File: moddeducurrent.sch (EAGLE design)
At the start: 29 parts, among them IC1 TLC251D, IC2 LMV321M5X, X1 USBPCB, X2 USBOLD

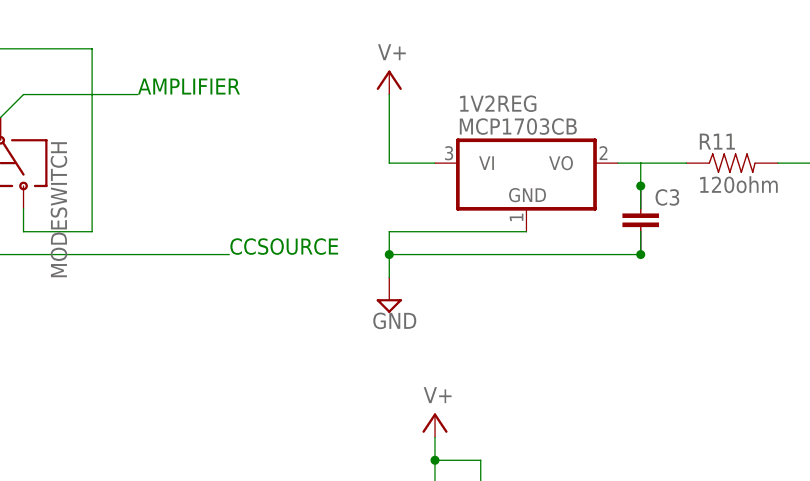
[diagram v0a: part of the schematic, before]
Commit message: Added missing input capacitor on 1V2REG just in case, fixed a piee of atrocious routing on the output cap of the same, beefed up the main current carrying trace.
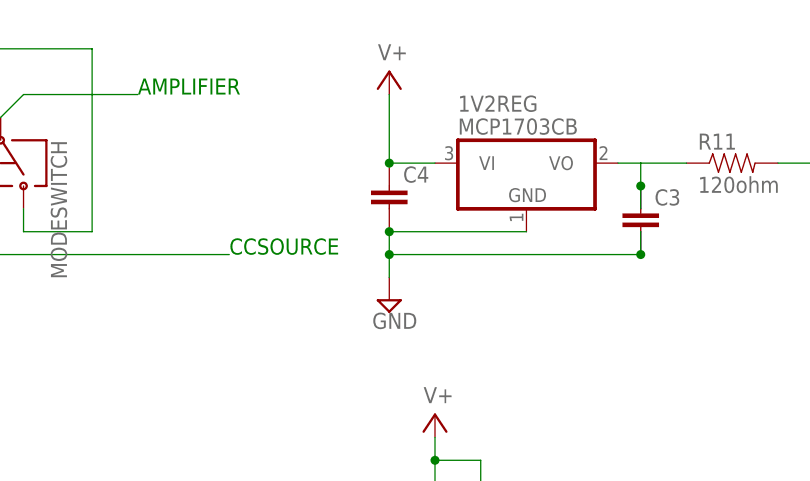
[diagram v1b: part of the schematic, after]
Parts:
- added C4: (no value), SparkFun - Copy:CAP0805
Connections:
- net GND: now also C4.2
- net V+: now also C4.1
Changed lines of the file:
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@@
 <part name="R12" library="SparkFun - Copy" deviceset="RESISTOR" device="0805-RES"/>
 <part name="S1" library="LL" deviceset="SWITCH-DP3T" device=""/>
+<part name="C4" library="SparkFun - Copy" deviceset="CAP" device="0805"/>
 </parts>
 <sheets>
@@
 <instance part="R12" gate="G$1" x="-27.94" y="101.6"/>
 <instance part="S1" gate="G$1" x="58.42" y="43.18"/>
+<instance part="C4" gate="G$1" x="132.08" y="121.92"/>
 </instances>
 <busses>
@@
 <pinref part="1V2REG" gate="G$1" pin="GND"/>
 <pinref part="SUPPLY10" gate="GND" pin="GND"/>
+<pinref part="C4" gate="G$1" pin="2"/>
+<junction x="132.08" y="119.38"/>
 </segment>
 <segment>
@@
 <pinref part="1V2REG" gate="G$1" pin="VI"/>
 <pinref part="SUPPLY7" gate="1" pin="V+"/>
-</segment>
-</net>
+<pinref part="C4" gate="G$1" pin="1"/>
+<junction x="132.08" y="127"/>
+</segment>
+</net>

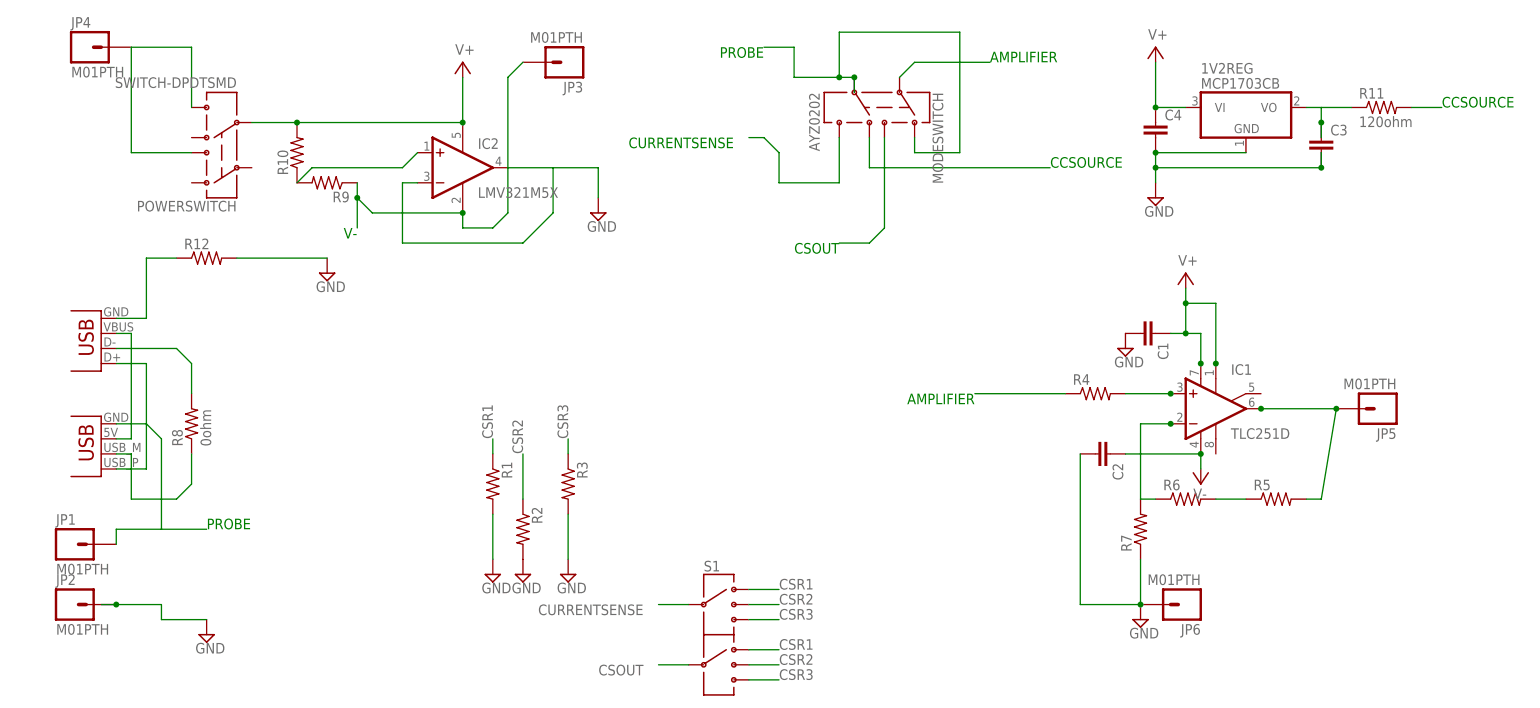
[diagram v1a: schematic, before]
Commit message: Changed switch to cheaper ebay switch. Added signal plane.
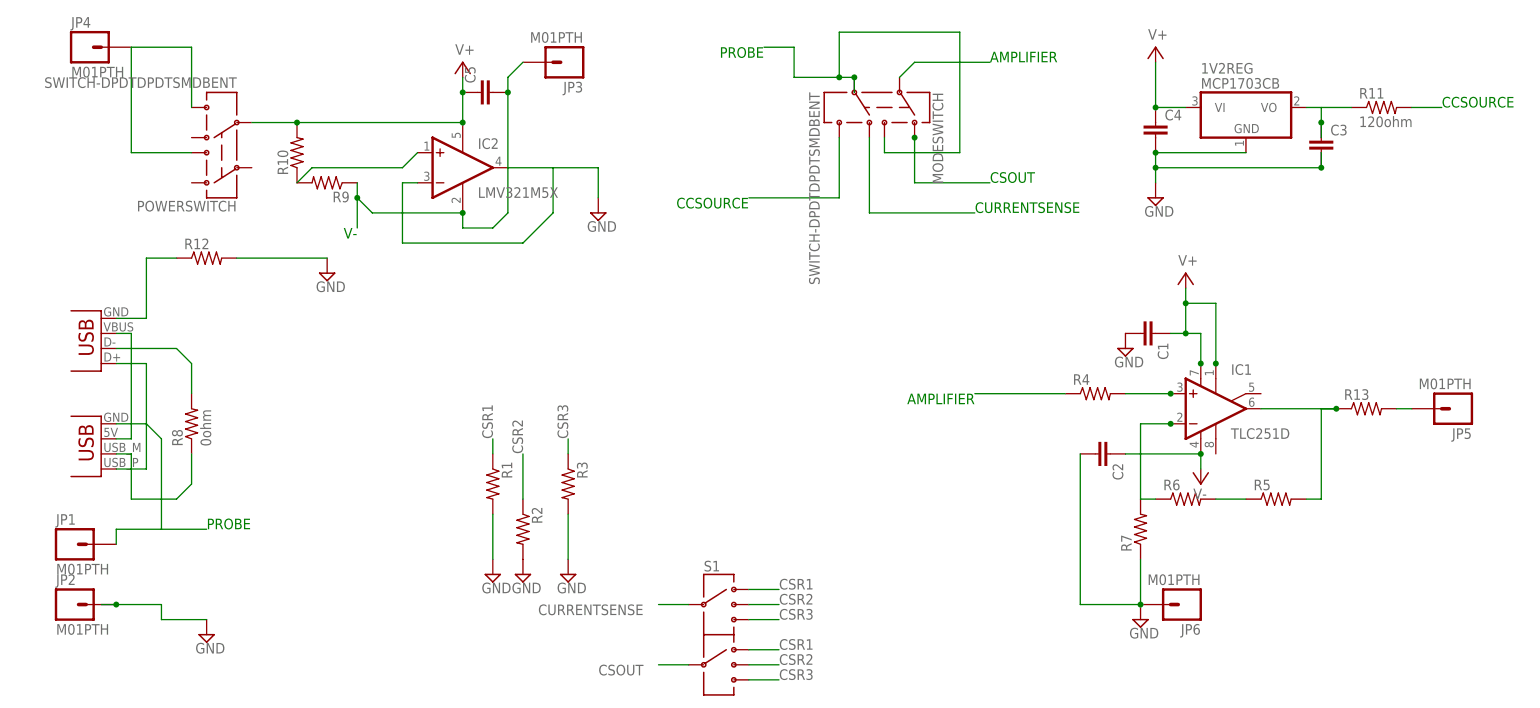
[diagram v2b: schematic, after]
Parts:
- added C5: (no value), SparkFun - Copy:CAP0805
- added R13: (no value), SparkFun - Copy:RESISTOR0805-RES
- MODESWITCH: value AYZ0202 -> SWITCH-DPDTDPDTSMDBENT; device SparkFun - Copy:AYZ0202 -> ebay:SWITCH-DPDTDPDTSMDBENT
- POWERSWITCH: value SWITCH-DPDTSMD -> SWITCH-DPDTDPDTSMDBENT; device SparkFun - Copy:SWITCH-DPDTSMD -> ebay:SWITCH-DPDTDPDTSMDBENT
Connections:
- new net N$2: JP5.1, R13.2
- net CCSOURCE: now also MODESWITCH.6; no longer MODESWITCH.4
- net CSOUT: now also MODESWITCH.1; no longer MODESWITCH.3
- net CURRENTSENSE: now also MODESWITCH.4; no longer MODESWITCH.6
- net OUT: now also R13.1; no longer JP5.1
- net PROBE: now also MODESWITCH.3; no longer MODESWITCH.1
- net V+: now also C5.1
- net V-: now also C5.2
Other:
- moved on the sheet: JP5

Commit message: added resistor values
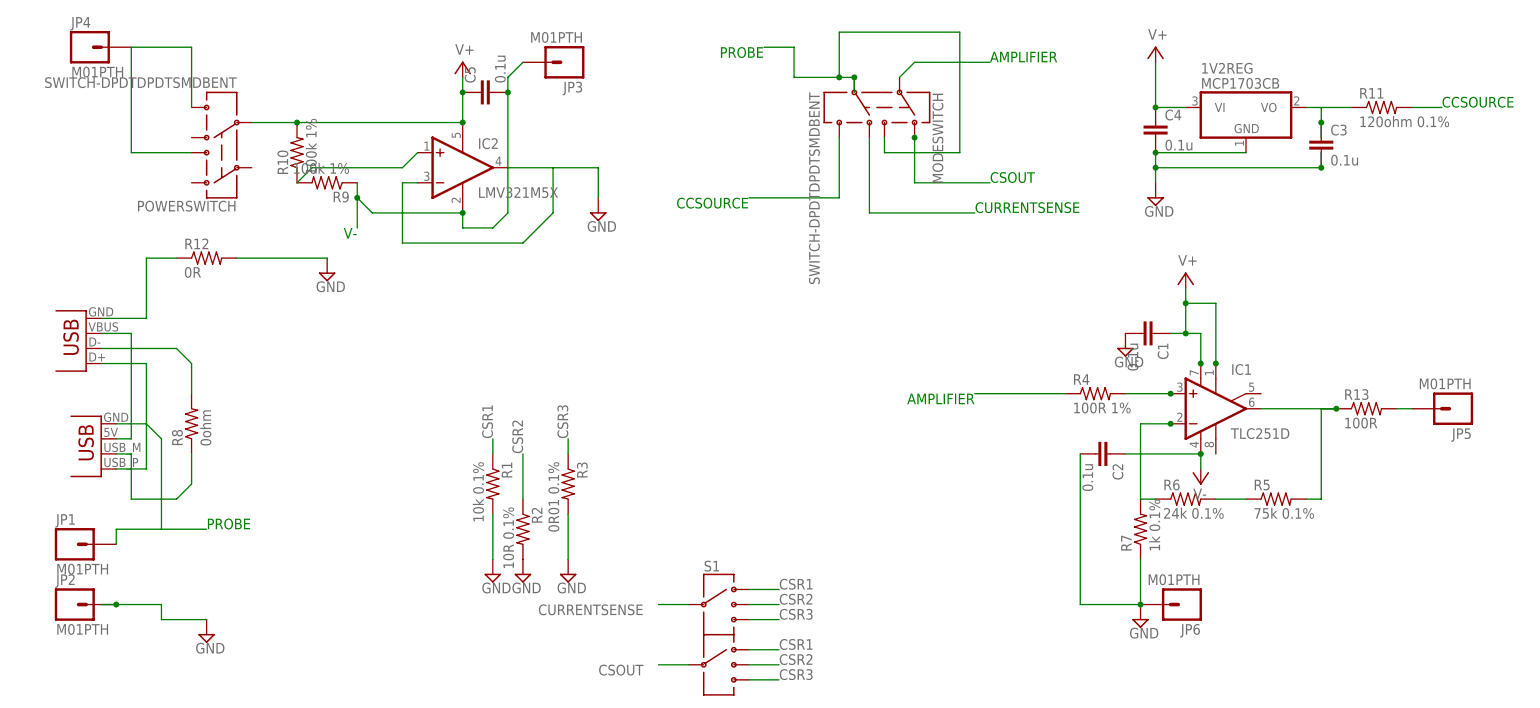
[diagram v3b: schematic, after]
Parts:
- C1, C2, C3, C4, C5: value (none) -> 0.1u
- R1: value (none) -> 10k 0.1%
- R10, R9: value (none) -> 100k 1%
- R11: value 120ohm -> 120ohm 0.1%
- R12: value (none) -> 0R
- R13: value (none) -> 100R
- R2: value (none) -> 10R 0.1%
- R3: value (none) -> 0R01 0.1%
- R4: value (none) -> 100R 1%
- R5: value (none) -> 75k 0.1%
- R6: value (none) -> 24k 0.1%
- R7: value (none) -> 1k 0.1%
